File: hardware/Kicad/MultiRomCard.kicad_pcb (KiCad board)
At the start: 2 copper layers, 160 x 100 mm, 17 parts, among them P1 VC4000_Cartridge_Bus, P2 MicroSD_Breakout, U1 Arduino_Nano, U2 74HC595, U3 74HC595, U4 74HC595, U5 6264, U6 74HC245, U7 74HC245, U8 74HC245

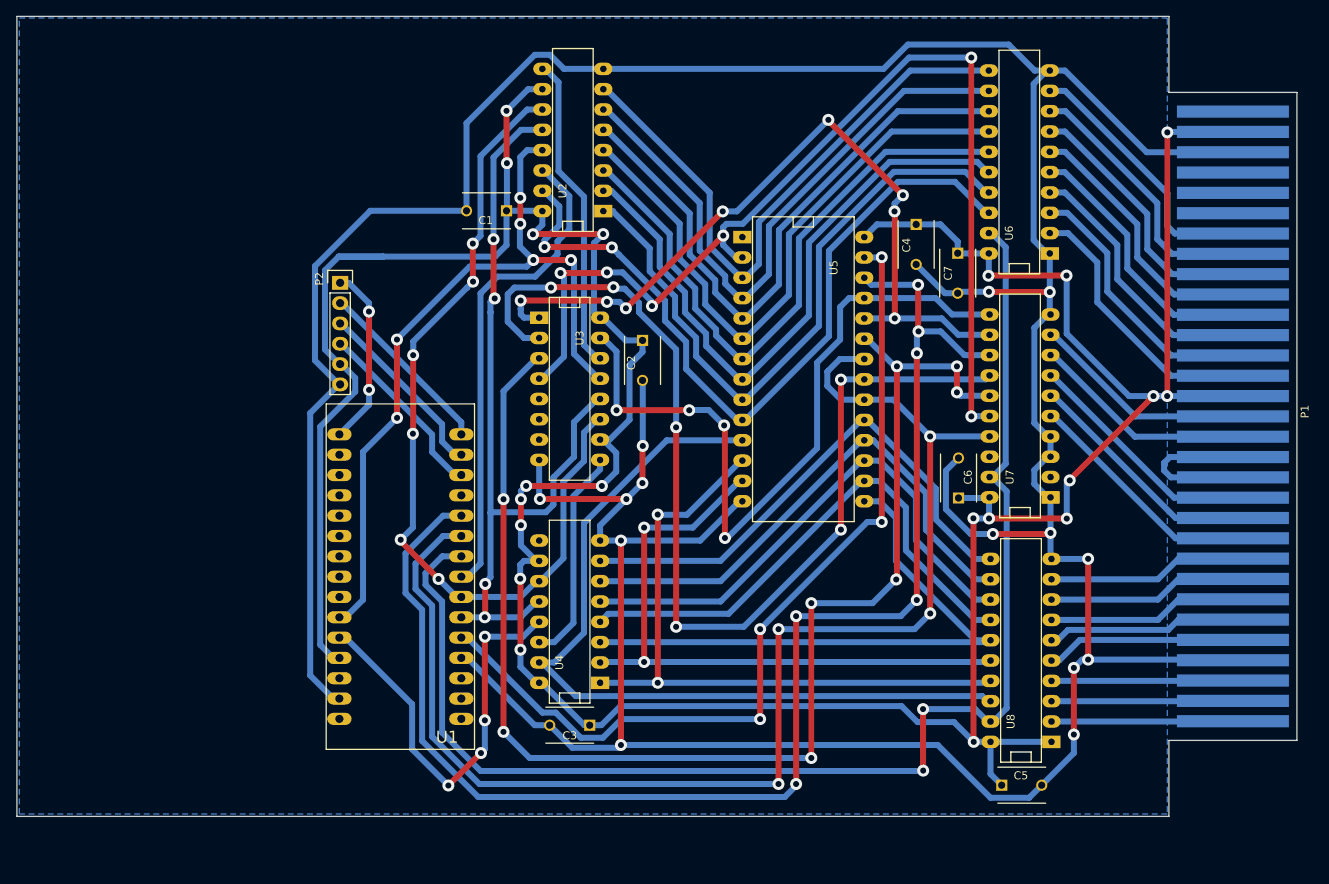
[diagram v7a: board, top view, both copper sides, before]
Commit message: [PCB] Shrink PCB to fit closer to the now used Arduino Nano.
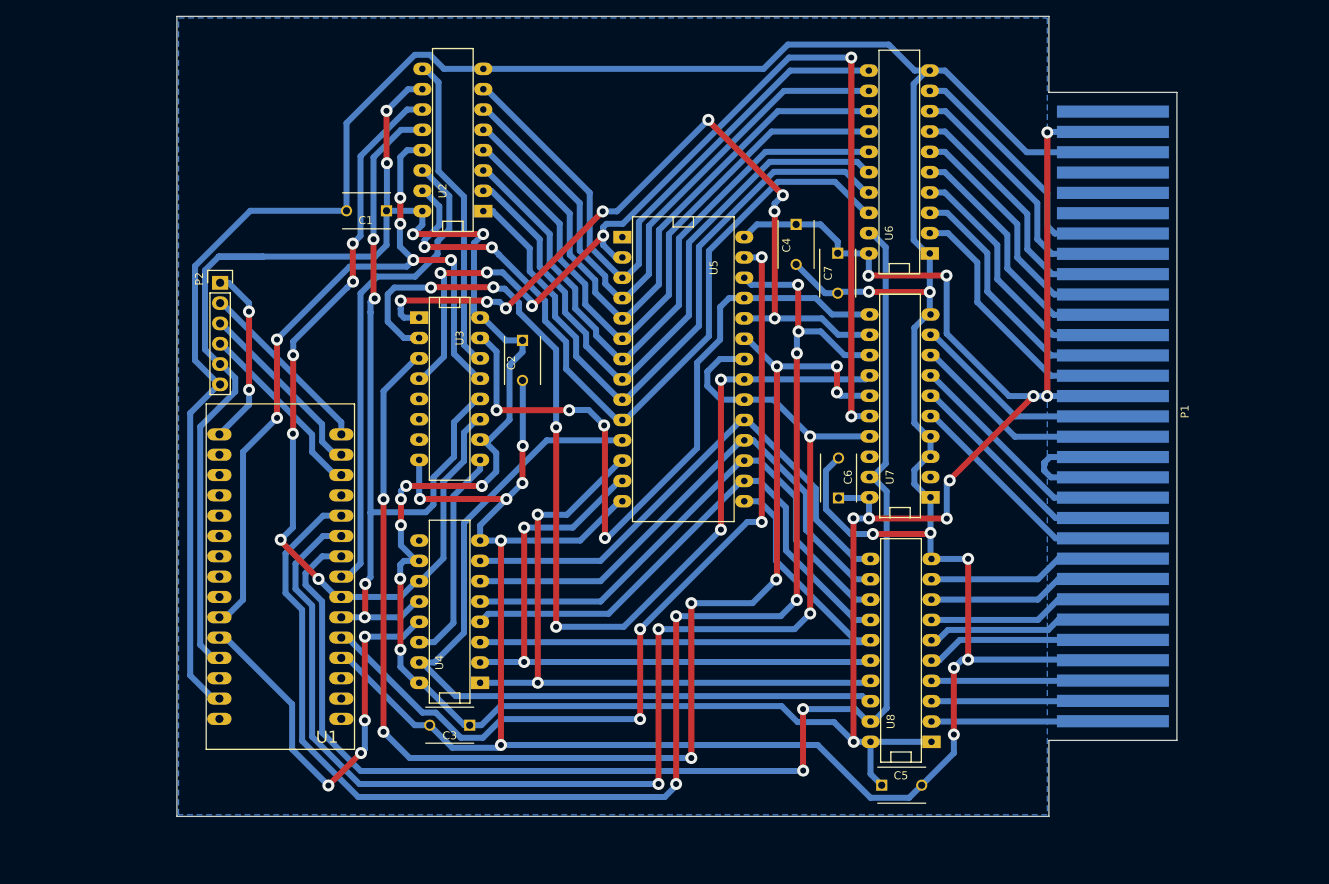
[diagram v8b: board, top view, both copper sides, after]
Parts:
- moved U2 15.0 mm to (120.5, 64.0)
- moved C1 15.0 mm to (112.2, 72.8)
- moved C2 15.0 mm to (129.2, 89.0)
- moved C3 15.0 mm to (122.6, 137.1)
- moved C4 15.0 mm to (163.4, 74.5)
- moved C5 15.0 mm to (174.1, 144.6)
- moved C6 15.0 mm to (168.7, 108.7)
- moved C7 15.0 mm to (168.6, 78.1)
- moved P1 15.0 mm to (203.0, 98.5)
- moved P2 15.0 mm to (91.4, 81.8)
- moved U1 15.0 mm to (106.5, 136.3)
- moved U3 15.0 mm to (120.1, 95.0)
- moved U4 15.0 mm to (120.1, 122.9)
- moved U5 15.0 mm to (149.3, 92.6)
- moved U6 15.0 mm to (176.3, 66.7)
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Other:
- board size 160 x 100 mm -> 125 x 100 mm
